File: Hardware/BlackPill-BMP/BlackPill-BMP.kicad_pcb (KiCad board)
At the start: 2 copper layers, 72.5 x 59.7 mm, 41 parts, among them J1 JTAG, J10 Conn_01x12_Male, J2 VCC, J3 GND, J4 SWO, J5 GDB_COMM, J6 TVCC, J7 LogicAna, J8 Conn_01x06_Male, J9 Conn_01x05_Male, U1 BlueAndBlackPill, U2 AD8531ARTZ, U3 74LVC2T45DC, U4 74LS126, U5 74LS126, U6 SRV05-4, U7 SRV05-4

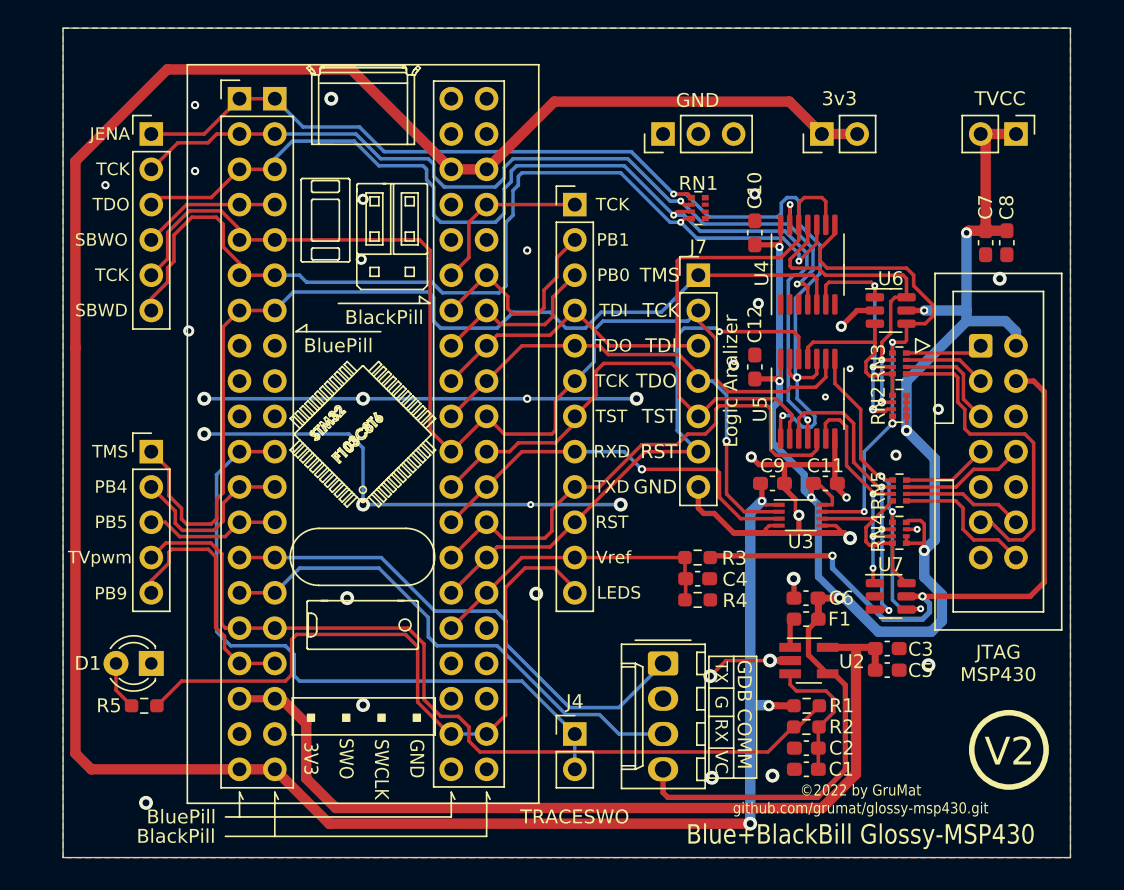
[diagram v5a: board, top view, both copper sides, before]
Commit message: Changed output buffer part#
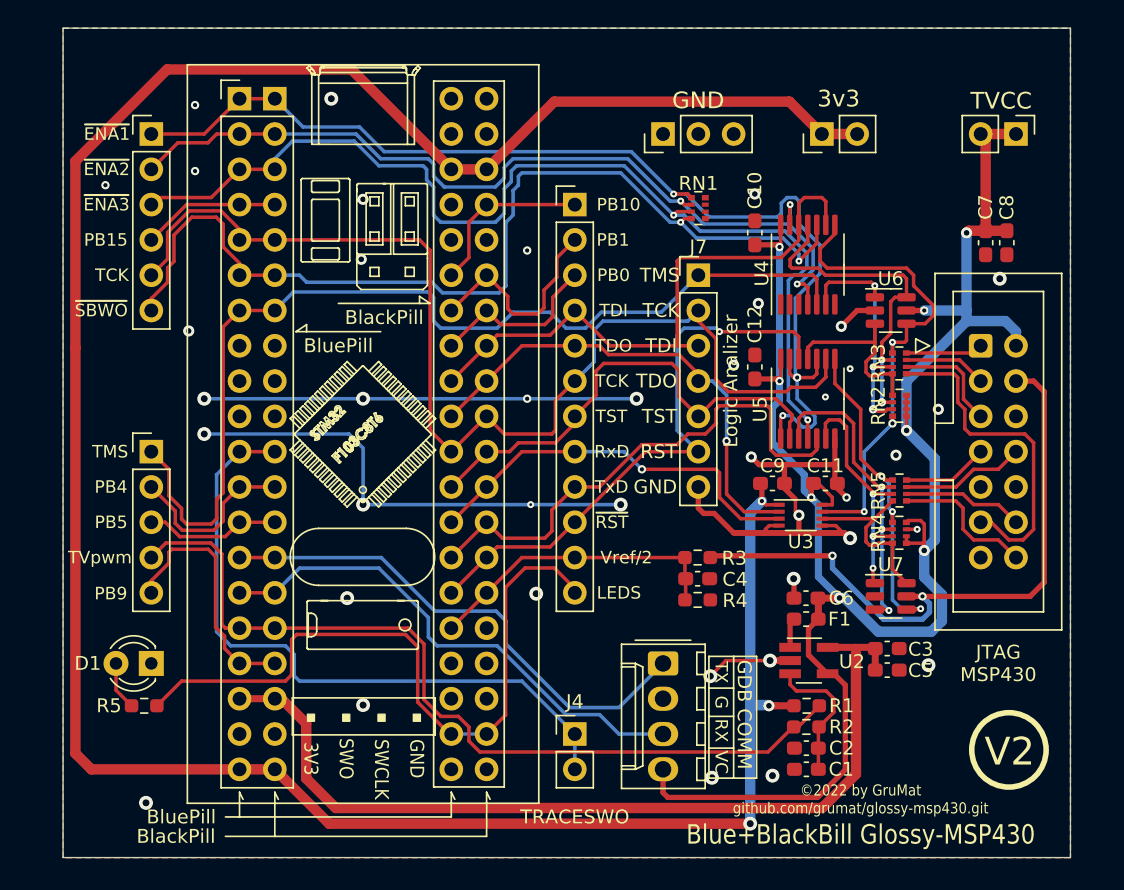
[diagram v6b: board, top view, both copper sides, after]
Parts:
- U4, U5: value 74LS126 -> 74LS125
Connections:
- net /ENA1 renamed /ENA1N
- net /ENA2 renamed /ENA2N
- net /ENA3 renamed /ENA3N
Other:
- board text added: "PB10"
- board text added: "PB15"
- board text added: "RxD"
- board text added: "TxD"
- board text added: "Vref/2"
- board text added: "~{ENA1}"
- board text added: "~{ENA2}"
- board text added: "~{ENA3}"
- board text added: "~{RST}"
- board text added: "~{SBWO}"
- board text removed: "JENA"
- board text removed: "RXD"
- board text removed: "SBWD"
- board text removed: "SBWO"
- board text removed: "TXD"
- board text removed: "Vref"
